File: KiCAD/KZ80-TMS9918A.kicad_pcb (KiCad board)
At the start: 2 copper layers, 100 x 75 mm, 42 parts, among them J1 Conn_Coaxial, J2 SBC8080 BUS, J3 EXT_JP, J4 AD_JP, J5 AD_JP, Q1 2SC1815, U1 74HCT04, U2 74HC139, U3 74HC32, U4 TMS9918A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

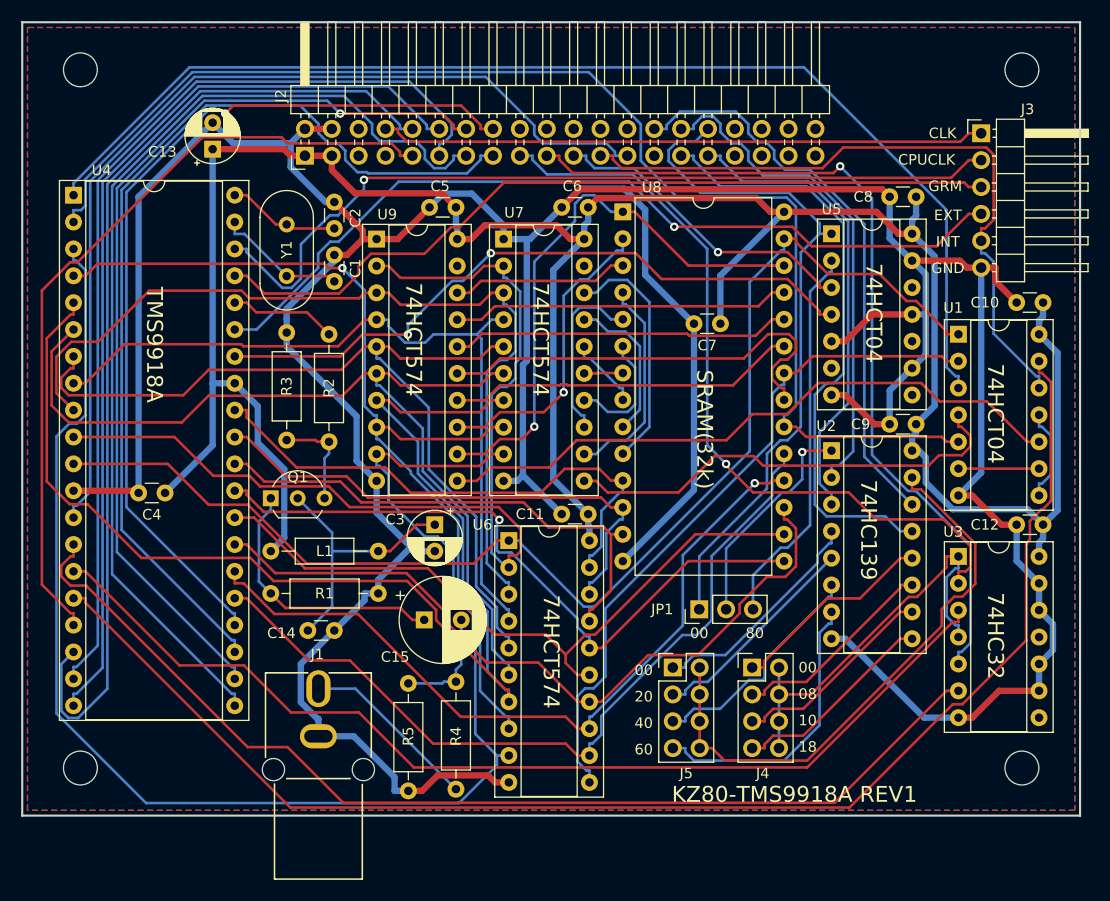
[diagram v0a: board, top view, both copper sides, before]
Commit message: パターンチェック後 SBCバスINT修正 、製造ファイル再出力
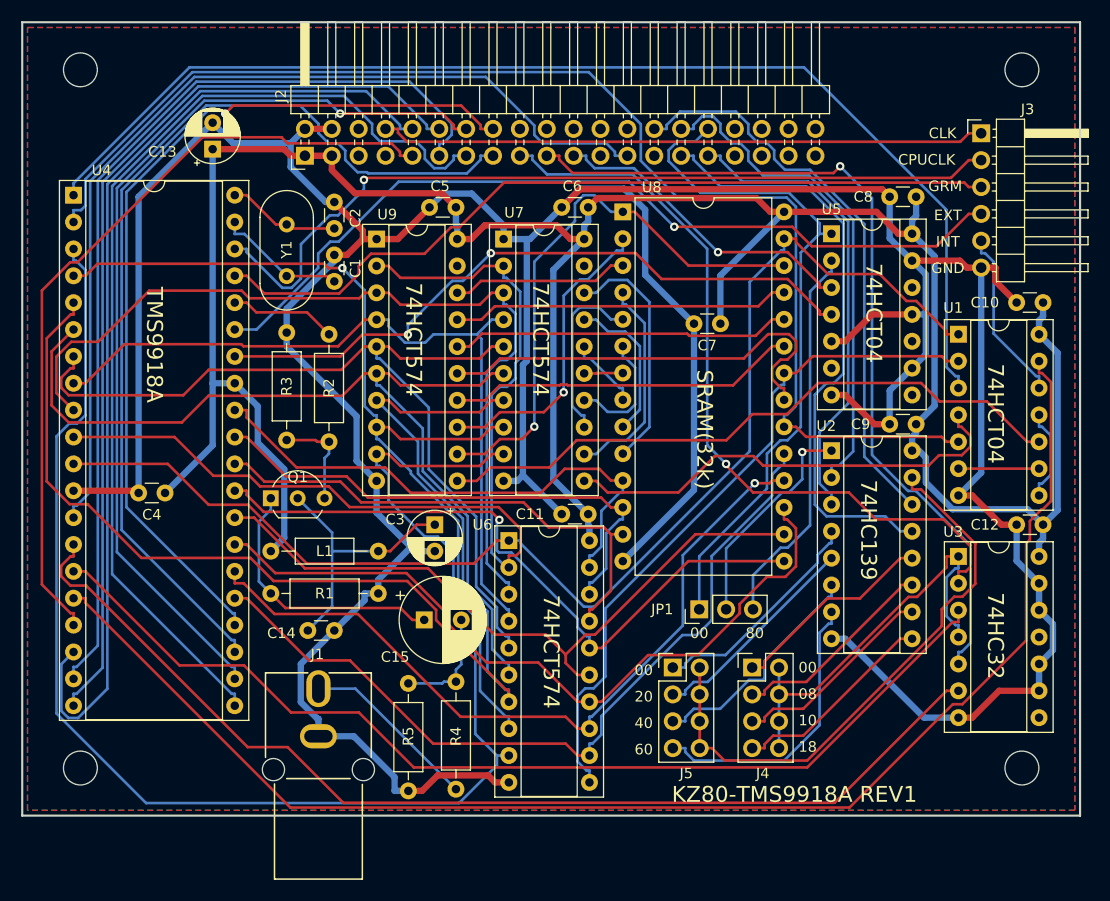
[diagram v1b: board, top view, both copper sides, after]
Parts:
- U6, U7, U9: value 74HC574 -> 74HCT574
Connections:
- J2 pad 23: /INT -> Net-(J2-Pad23)
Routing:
- net /INT: track 64.4 -> 16.6 mm

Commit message: 回路見直し&パターン再作成
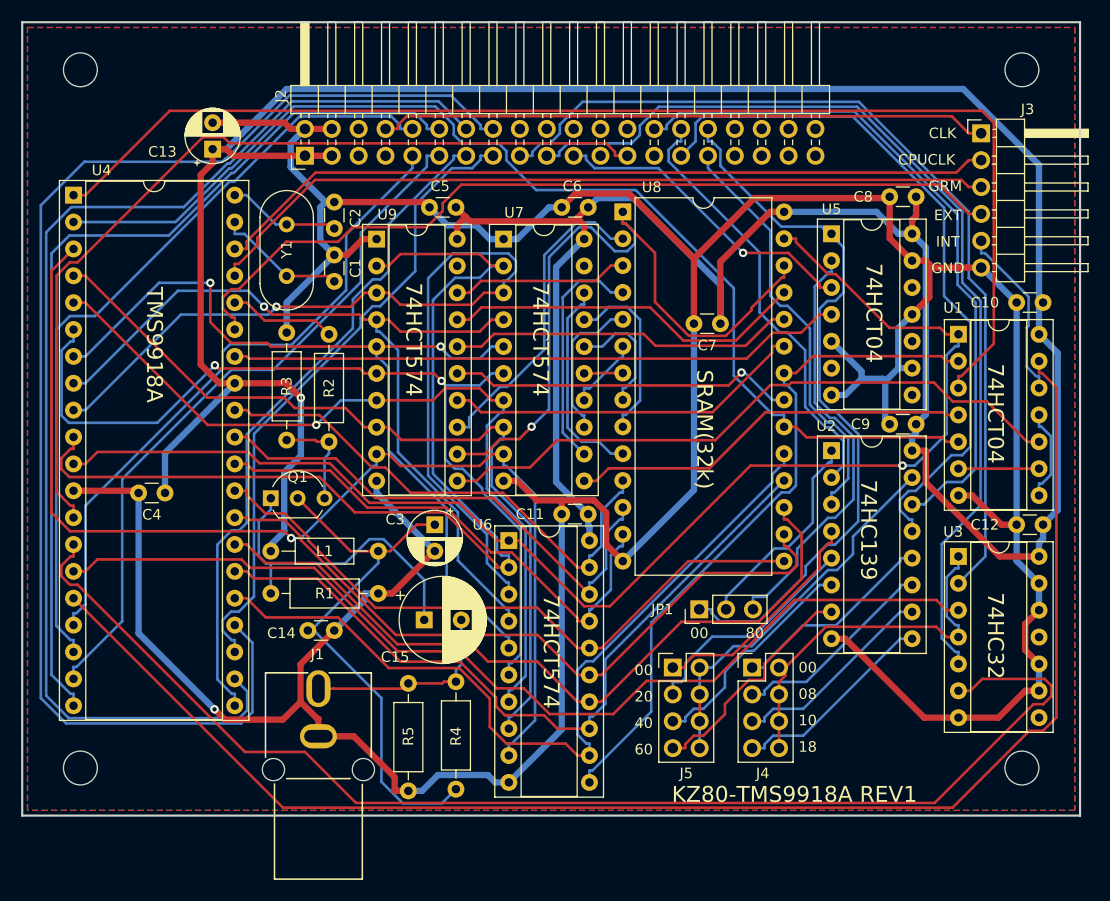
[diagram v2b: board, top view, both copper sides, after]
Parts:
- R1: value 300 -> 180
- R4: value 75 -> 1k
- R5: value 10k -> 2k
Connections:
- J1 pad 1: Net-(J1-Pad1) -> Net-(C15-Pad2)
- R4 pad 1: Net-(J1-Pad1) -> Net-(C14-Pad1)
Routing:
- net VCC: track 245.2 -> 333.2 mm, vias 0 -> 1
- net /D7: track 84.7 -> 125.5 mm, vias 1 -> 0
- net /AD5: track 118.4 -> 79.0 mm, vias 0 -> 1
- net /AD7: track 141.8 -> 105.5 mm, vias 0 -> 1
- net /D4: track 95.6 -> 64.1 mm
- net /D6: track 91.3 -> 60.8 mm
- net Net-(C14-Pad1): track 25.5 -> 52.1 mm
- net /D5: track 88.9 -> 113.3 mm, vias 1 -> 0
- net /D2: track 90.9 -> 66.9 mm
- net GND: track 411.9 -> 388.7 mm, vias 0 -> 1
- net /D1: track 93.7 -> 74.0 mm
- net /~CSW: track 101.7 -> 120.8 mm
- net Net-(J5-Pad2): track 55.0 -> 36.1 mm
- net Net-(J1-Pad1): track 16.9 -> 0.00 mm
- net /~CAS: track 122.1 -> 107.9 mm
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
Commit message: INT端子ジャンパ装備 パターン再作成、ガーバー出力
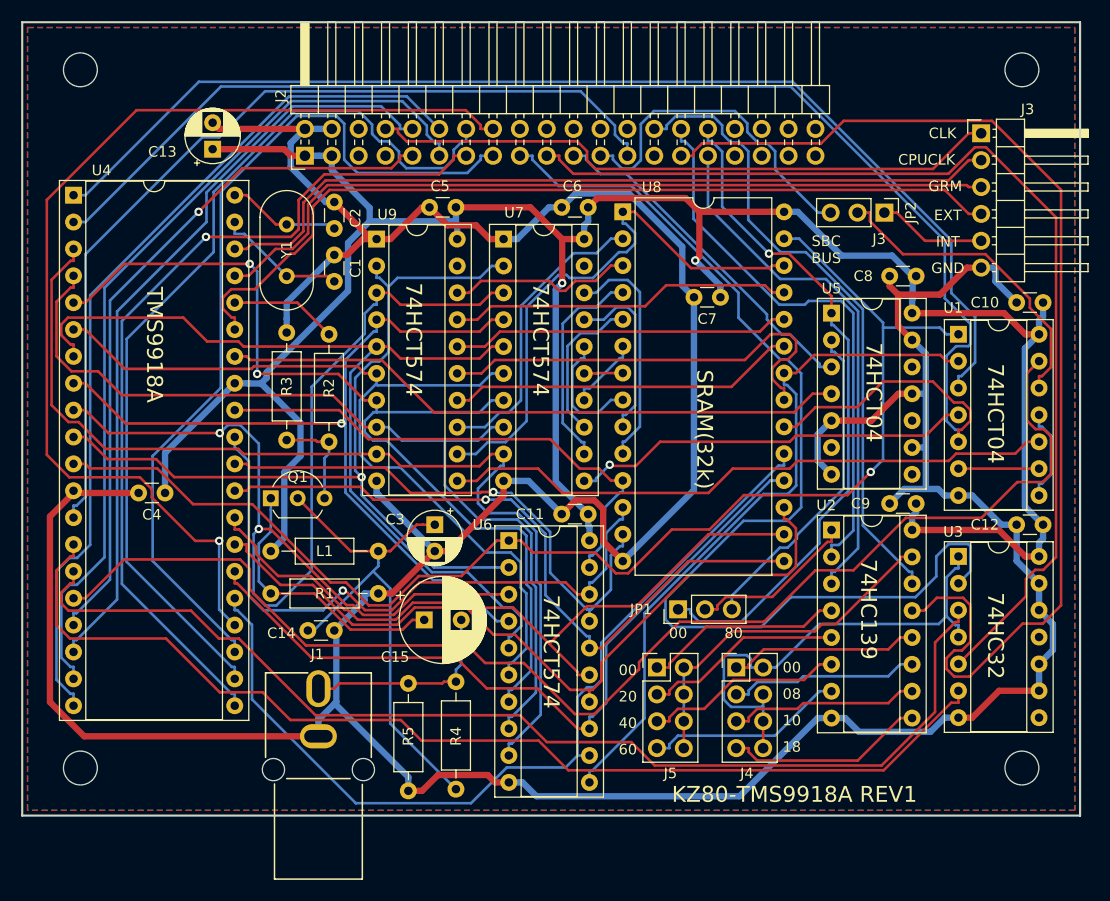
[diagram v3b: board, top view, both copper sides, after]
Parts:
- added JP2: INT-J, Connector_PinHeader_2.54mm:PinHeader_1x03_P2.54mm_Vertical, F.Cu at (181.5, 68.0)
- moved C8 7.50 mm to (184.5, 74.0)
- moved C9 7.50 mm to (184.5, 95.5)
- moved U2 7.50 mm to (176.5, 98.0)
- moved U5 7.50 mm to (176.5, 77.5)
- moved C7 2.50 mm to (166.0, 76.0)
- moved JP1 2.00 mm to (162.0, 105.5)
- moved J4 1.50 mm to (167.5, 111.0)
- moved J5 1.50 mm to (160.0, 111.0)
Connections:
- J2 pad 23: Net-(J2-Pad23) -> /INT80
- U1 pad 12: /INT -> Net-(JP2-Pad2)
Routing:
- net VCC: track 333.2 -> 232.0 mm, vias 1 -> 2
- net /A4: track 67.0 -> 107.1 mm
- net /~CAS: track 107.9 -> 140.1 mm
- net /INT80: track 0.00 -> 32.2 mm
- net Net-(JP2-Pad2): track 0.00 -> 30.0 mm
- net /D5: track 113.3 -> 86.9 mm
- net /D7: track 125.5 -> 99.4 mm, vias 0 -> 1
- net /D6: track 60.8 -> 83.4 mm
- net /~IOR: track 86.4 -> 105.3 mm
- net /AD1: track 92.6 -> 110.8 mm, vias 1 -> 2
- net /AD0: track 99.6 -> 81.5 mm, vias 0 -> 1
- net /D4: track 64.1 -> 81.8 mm, vias 0 -> 1
- net /~CSW: track 120.8 -> 103.2 mm
- net /~INT: track 139.2 -> 123.4 mm
- net /D2: track 66.9 -> 82.0 mm
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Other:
- board text added: "J3"
- board text added: "SBC BUS"
